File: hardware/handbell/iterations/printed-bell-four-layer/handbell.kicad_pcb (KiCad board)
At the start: 4 copper layers, 44.5 x 48.3 mm, 104 parts, among them IC1 RP2040_QFN56, IC4 LSM6DSOXTR, J1 504050-0291, J2 SM02B-SRSS-TB, Q1 AO3401, Q2 AO3400A, Q3 DMP2045UFY4, Q4 AO3400A, Q5 CSD83325L, U1 W25Q16JVUXIQ TR / 2MB, U2 RT9080-3.3, U3 MCP73831T-2ACI/OT, U4 MAX98357A, U5 TPS61023DRLR, U6 BQ29700DSER, X6 USB Type C, Y1 12MHz/CL10pF

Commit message: Accept first protected inner-ground plane routing baseline
Resume owner-authorized work; promote exact reviewed candidate and rebind manifest metadata. Preserve 137 prior groups and private returns, reduce opens from 51 to 49, retain source-bound native whitespace and all pending qualification gates.

Co-authored-by: Copilot <223556219+Copilot@users.noreply.github.com>
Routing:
- added copper zone on In1.Cu, net GND

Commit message: Connect 3V3 groups through existing vias on In2
Accept exact 0.4mm supply bridge, preserve all prior copper and planes, bind source evidence and release bounded local supply-ground stitches. 48 opens remain.

Co-authored-by: Copilot <223556219+Copilot@users.noreply.github.com>
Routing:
- net +3V3: track 168.4 -> 178.3 mm
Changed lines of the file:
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@@
         (polygon (pts (xy 90.103600 96.152596) (xy 97.237500 96.152596) (xy 97.237500 100.263901) (xy 90.103600 100.263901)))
     )
+(segment (start 92.850000 93.350000) (end 93.750000 94.250000) (width 0.400000) (layer "In2.Cu") (net "+3V3"))
+(segment (start 93.750000 94.250000) (end 100.557500 94.250000) (width 0.400000) (layer "In2.Cu") (net "+3V3"))
+(segment (start 100.557500 94.250000) (end 101.802000 93.005500) (width 0.400000) (layer "In2.Cu") (net "+3V3"))
 )

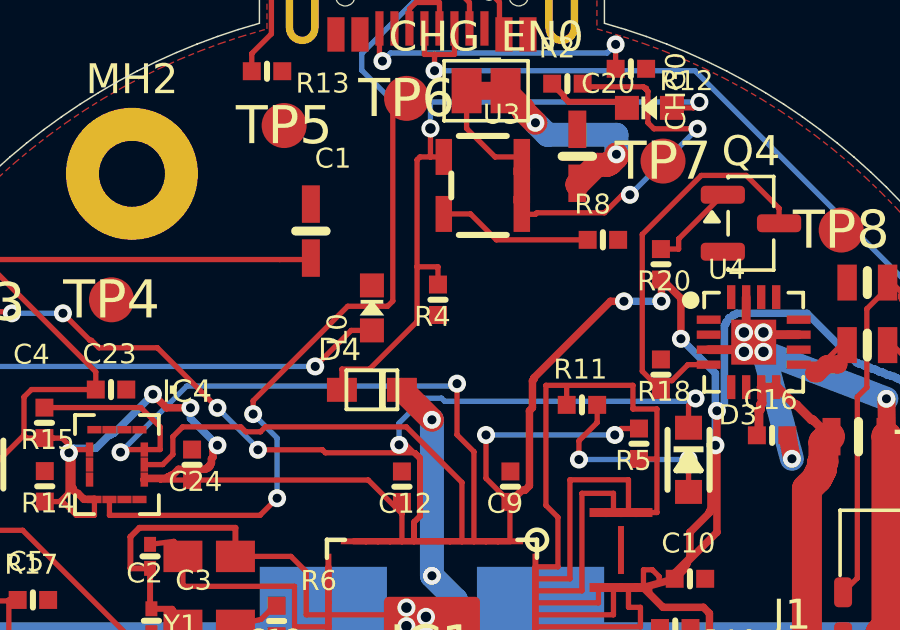
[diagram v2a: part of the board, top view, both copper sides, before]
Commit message: Accept validated R4 ground stitch and preserve native API controls
Promote exact saved candidate: 47 opens, unchanged F/In1 fill, preserved private returns and connected groups. Keep C9 local high-frequency return unqualified and historical validator failures intact.

Co-authored-by: Copilot <223556219+Copilot@users.noreply.github.com>
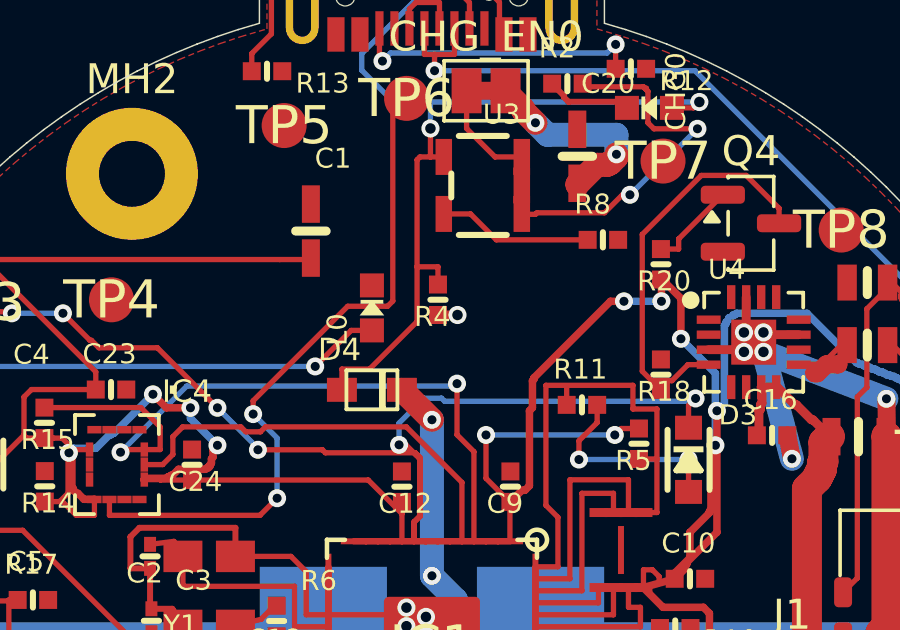
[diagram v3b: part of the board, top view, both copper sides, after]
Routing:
- net GND: track 114.1 -> 114.7 mm, vias 19 -> 20
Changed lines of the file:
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@@
 (segment (start 93.750000 94.250000) (end 100.557500 94.250000) (width 0.400000) (layer "In2.Cu") (net "+3V3"))
 (segment (start 100.557500 94.250000) (end 101.802000 93.005500) (width 0.400000) (layer "In2.Cu") (net "+3V3"))
+(segment (start 100.201085 89.006710) (end 100.851085 89.006710) (width 0.300000) (layer "F.Cu") (net "GND"))
+(via (at 100.851085 89.006710) (size 0.604000) (drill 0.350000) (layers "F.Cu" "B.Cu") (net "GND"))
 )

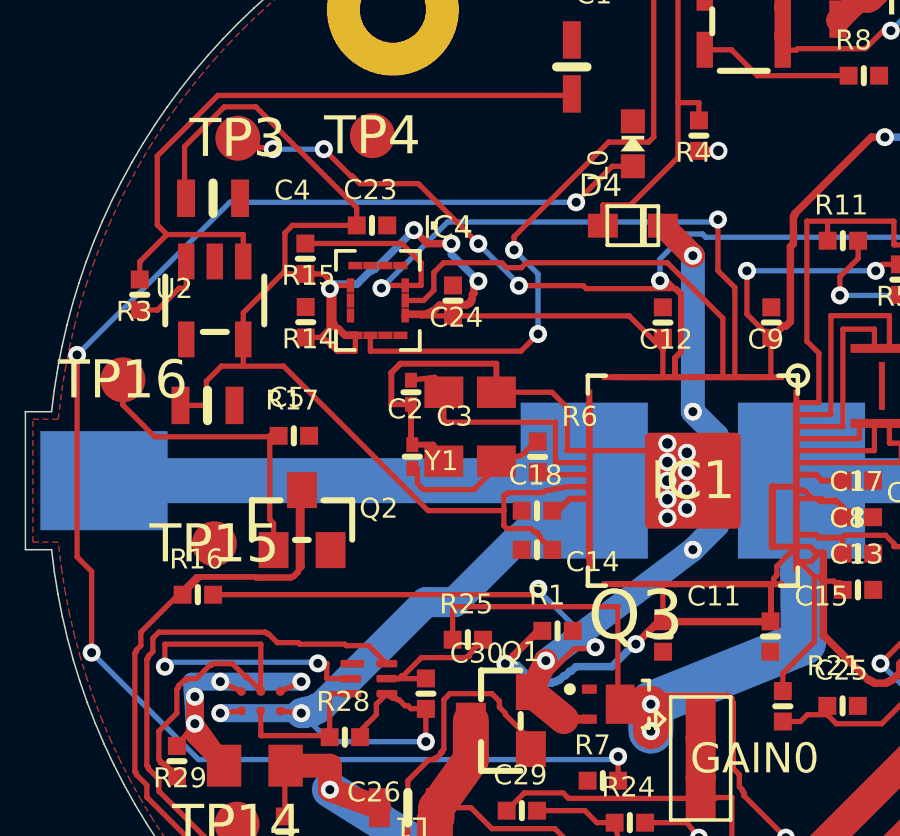
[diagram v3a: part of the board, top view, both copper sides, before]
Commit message: Connect three supply-ground groups with validated local stitches
Promote exact radial batch: 44 opens, unchanged planes and existing routing, preserved private returns. Retain finite C12/C23/C24 blockers and qualification limits.

Co-authored-by: Copilot <223556219+Copilot@users.noreply.github.com>
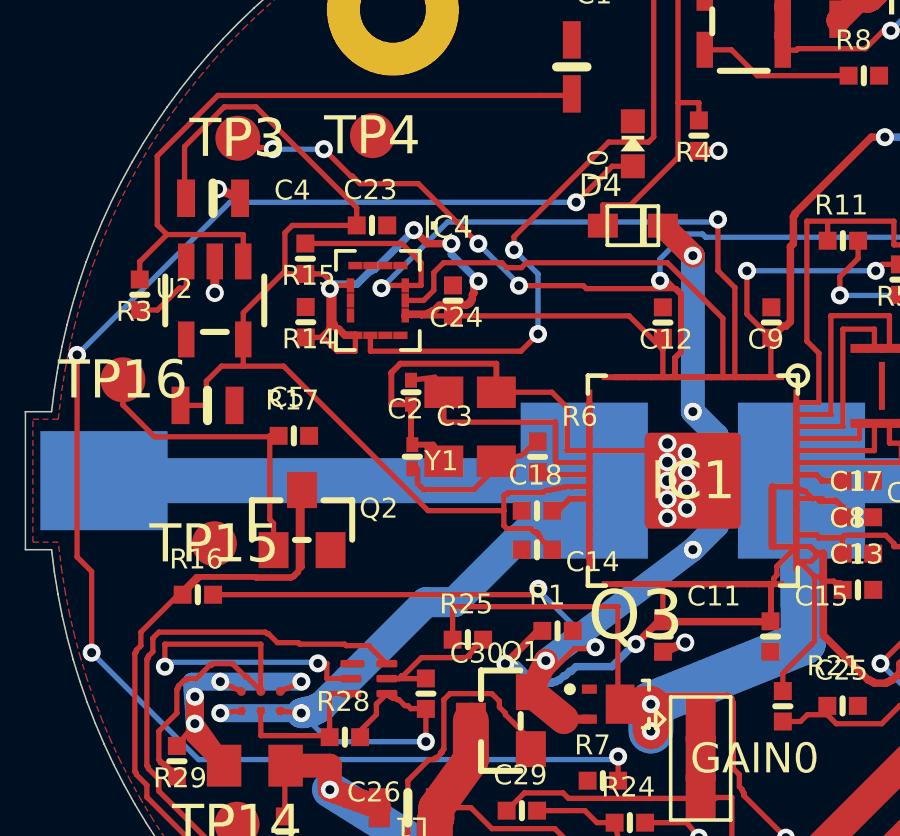
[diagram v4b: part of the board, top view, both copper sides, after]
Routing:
- net GND: track 114.7 -> 117.4 mm, vias 20 -> 23
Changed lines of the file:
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@@
 (segment (start 100.201085 89.006710) (end 100.851085 89.006710) (width 0.300000) (layer "F.Cu") (net "GND"))
 (via (at 100.851085 89.006710) (size 0.604000) (drill 0.350000) (layers "F.Cu" "B.Cu") (net "GND"))
+(segment (start 84.906419 90.585985) (end 84.167315 90.279838) (width 0.300000) (layer "F.Cu") (net "GND"))
+(via (at 84.167315 90.279838) (size 0.604000) (drill 0.350000) (layers "F.Cu" "B.Cu") (net "GND"))
+(segment (start 99.005927 105.703623) (end 99.745031 105.397476) (width 0.300000) (layer "F.Cu") (net "GND"))
+(via (at 99.745031 105.397476) (size 0.604000) (drill 0.350000) (layers "F.Cu" "B.Cu") (net "GND"))
+(segment (start 84.063240 92.692100) (end 84.063240 93.742100) (width 0.300000) (layer "F.Cu") (net "GND"))
+(via (at 84.063240 93.742100) (size 0.604000) (drill 0.350000) (layers "F.Cu" "B.Cu") (net "GND"))
 )
